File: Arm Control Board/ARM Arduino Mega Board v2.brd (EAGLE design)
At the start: 189.8 x 119.2 mm, 58 parts, among them IC1 7805TV

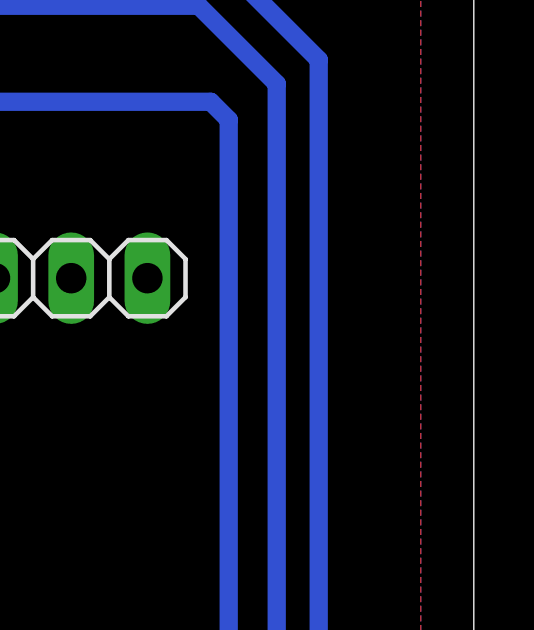
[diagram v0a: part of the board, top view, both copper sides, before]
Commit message: updated plane thickness
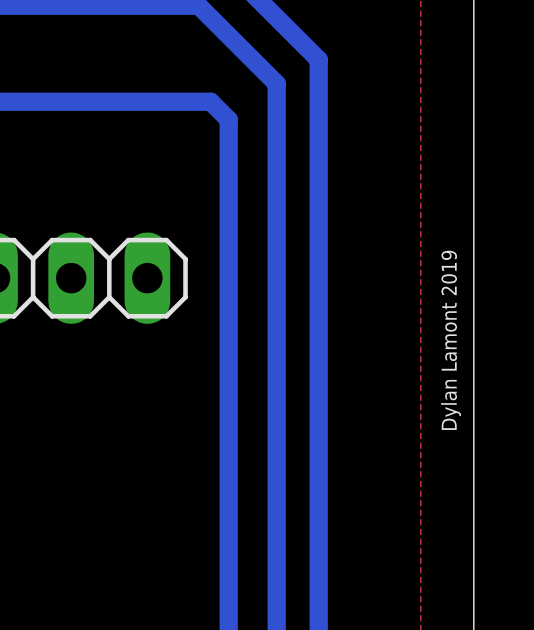
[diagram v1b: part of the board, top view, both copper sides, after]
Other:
- board text added: "Dylan Lamont 2019"
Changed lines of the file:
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@@
 <wire x1="74.2" y1="104.6" x2="58.8" y2="104.6" width="0.4064" layer="25"/>
 <wire x1="58.8" y1="104.6" x2="58.8" y2="114.8" width="0.4064" layer="25"/>
+<text x="185.2" y="94" size="0.5" layer="25" rot="R90">Dylan Lamont 2019</text>
 </plain>
 <attributes>
@@
 <wire x1="10" y1="74.2" x2="7.57" y2="74.2" width="0.4064" layer="1"/>
 <wire x1="7.57" y1="74.2" x2="7.08" y2="73.71" width="0.4064" layer="1"/>
-<polygon width="0.4064" layer="16" isolate="0.6096">
+<polygon width="1.27" layer="16" isolate="0.6096">
 <vertex x="-2" y="118"/>
 <vertex x="183" y="118"/>
@@
 <contactref element="M-6" pad="8"/>
 <contactref element="M-6" pad="7"/>
-<polygon width="0.4064" layer="1" isolate="0.6096">
+<polygon width="1.27" layer="1" isolate="0.6096">
 <vertex x="-3" y="118"/>
 <vertex x="183" y="118"/>

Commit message: Gerbers added for drive board and arm control pcb
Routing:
- net OUTA1: track 85.2 -> 87.4 mm
- net OUTA2: track 51.0 -> 49.2 mm
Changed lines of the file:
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@@
 <contactref element="C1" pad="2"/>
 <contactref element="U$3" pad="PIN1"/>
+<wire x1="169.95" y1="66.8" x2="157.2" y2="67.4" width="0" layer="19" extent="1-1"/>
 </signal>
 <signal name="D35">
@@
 <contactref element="M-6" pad="8"/>
 <contactref element="M-6" pad="7"/>
-<polygon width="1.27" layer="1" isolate="0.6096">
+<polygon width="1.27" layer="1" isolate="0.8128">
 <vertex x="-3" y="118"/>
 <vertex x="183" y="118"/>
@@
 <wire x1="46" y1="107.2" x2="78.2" y2="107.2" width="2.1844" layer="16"/>
 <wire x1="78.2" y1="107.2" x2="78.6" y2="107.6" width="2.1844" layer="16"/>
-<wire x1="78.6" y1="107.6" x2="78.6" y2="112.2" width="2.1844" layer="16"/>
-<wire x1="78.6" y1="112.2" x2="79.4" y2="113" width="2.1844" layer="16"/>
-<wire x1="79.4" y1="113" x2="82.4" y2="113" width="2.1844" layer="16"/>
-<wire x1="82.4" y1="113" x2="82.5" y2="112.1" width="2.1844" layer="16"/>
+<wire x1="78.6" y1="107.6" x2="78.6" y2="110.8" width="2.1844" layer="16"/>
+<wire x1="78.6" y1="110.8" x2="79.4" y2="111.4" width="2.1844" layer="16"/>
+<wire x1="79.4" y1="111.4" x2="82.4" y2="111.4" width="2.1844" layer="16"/>
+<wire x1="82.4" y1="111.4" x2="82.5" y2="112.1" width="2.1844" layer="16"/>
 <wire x1="42.27" y1="99.12" x2="44.81" y2="99.12" width="0" layer="19" extent="1-1"/>
 </signal>
@@
 <contactref element="U$2" pad="PIN5"/>
 <wire x1="19.81" y1="99.12" x2="19.81" y2="106.61" width="2.1844" layer="16"/>
-<wire x1="19.81" y1="106.61" x2="27.4" y2="114.4" width="2.1844" layer="16"/>
-<wire x1="27.4" y1="114.4" x2="89.4" y2="114.4" width="2.1844" layer="16"/>
-<wire x1="89.4" y1="114.4" x2="89.4" y2="113.2" width="2.1844" layer="16"/>
+<wire x1="19.81" y1="106.61" x2="29.2" y2="116" width="2.1844" layer="16"/>
+<wire x1="29.2" y1="116" x2="89.4" y2="116" width="2.1844" layer="16"/>
+<wire x1="89.4" y1="116" x2="89.4" y2="113.2" width="2.1844" layer="16"/>
 <wire x1="89.4" y1="113.2" x2="89.5" y2="112.1" width="2.1844" layer="16"/>
 </signal>
